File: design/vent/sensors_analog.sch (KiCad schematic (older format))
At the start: 11 parts, among them J14 Conn_01x02, J15 Conn_01x02, J16 Conn_01x03, J17 Conn_01x02, J18 Conn_01x02, U10 SPU01M-15

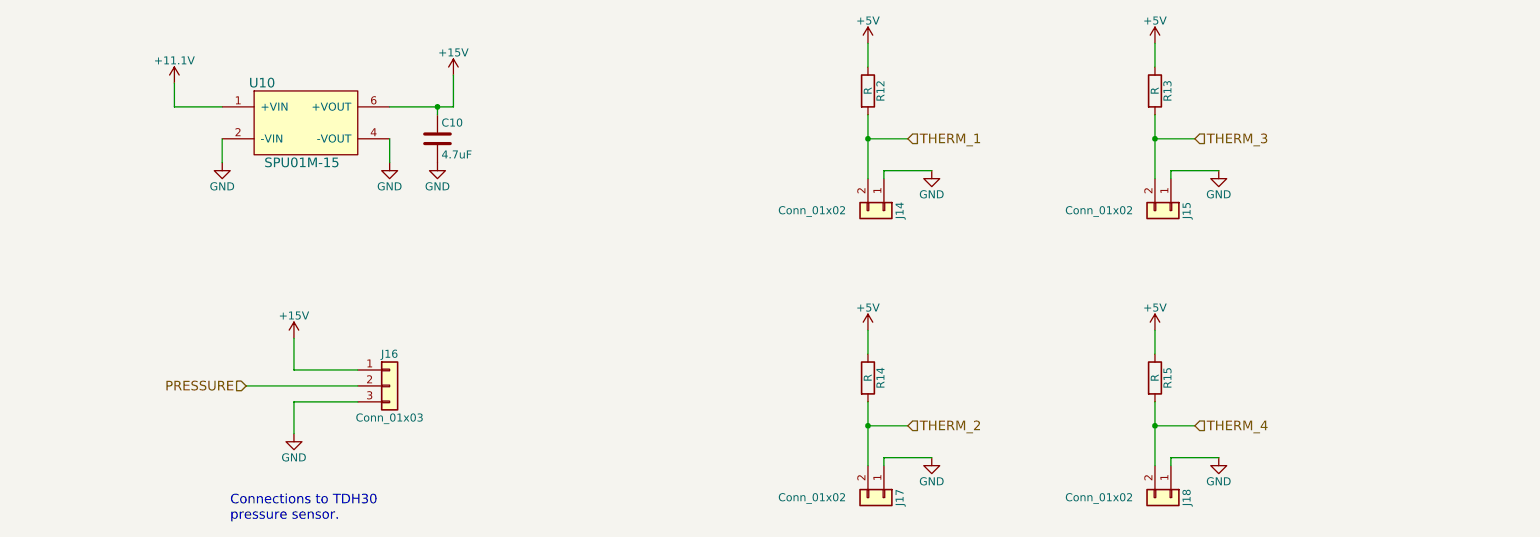
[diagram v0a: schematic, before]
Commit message: Refine schematic
- Add part numbers and correct pinout for mosfets
- Add fuses to battery inputs
- Add decoupling caps to logic translators
- Add flyback diodes to H Bridge, to be populated if the body diodes of
  the mosfets are not sufficient.
- Change H Bridge to operate with 4 inputs instead of 2.

Also, misc directory cleanup.
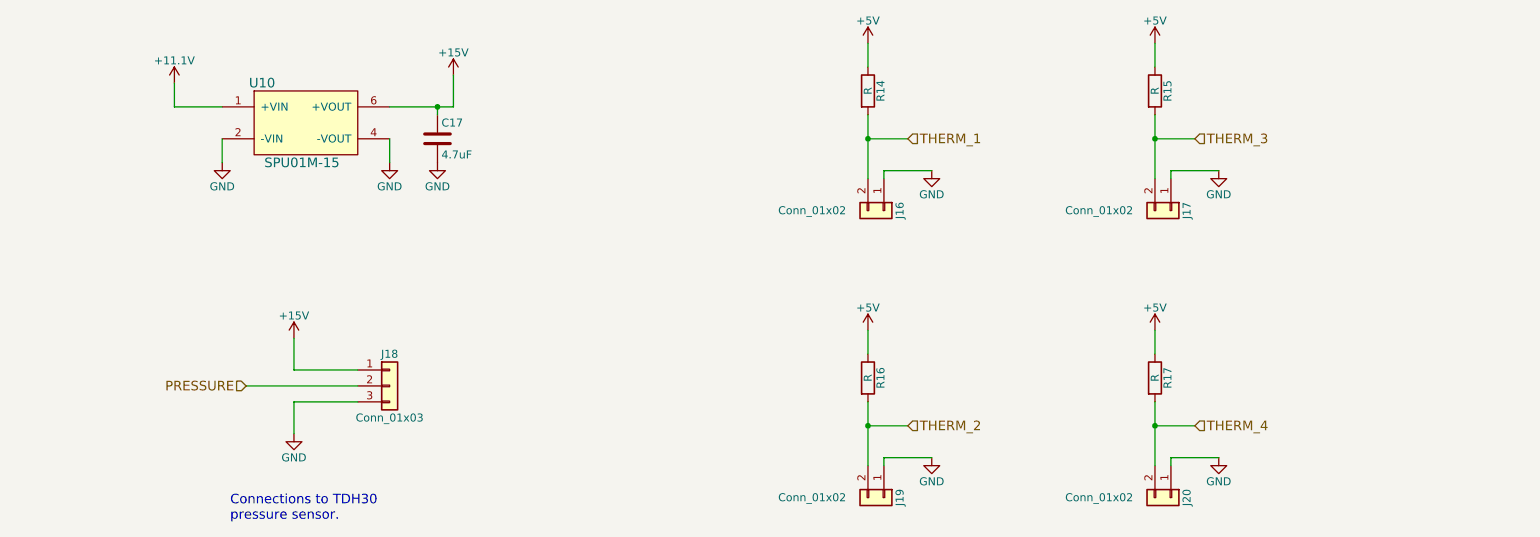
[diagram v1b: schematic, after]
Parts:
- renumbered C10 to C17, J14 to J16, J15 to J17, J16 to J18, J17 to J19, J18 to J20, R12 to R14, R13 to R15, R14 to R16, R15 to R17
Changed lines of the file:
@@
 $EndDescr
 $Comp
-L Conn_01x02 J14
+L Conn_01x02 J16
 U 1 1 5AE81751
 P 6800 3150
-F 0 "J14" H 6800 3250 50  0000 C CNN
+F 0 "J16" H 6800 3250 50  0000 C CNN
 F 1 "Conn_01x02" V 6800 2700 50  0000 C CNN
 F 2 "Connectors_Phoenix:PhoenixContact_MCV-G_02x3.50mm_Vertical" H 6800 3150 50  0001 C CNN
@@
 $EndComp
 $Comp
-L R R12
+L R R14
 U 1 1 5AE81758
 P 6700 2400
-F 0 "R12" V 6780 2400 50  0000 C CNN
+F 0 "R14" V 6780 2400 50  0000 C CNN
 F 1 "R" V 6700 2400 50  0000 C CNN
 F 2 "Resistors_ThroughHole:R_Axial_DIN0207_L6.3mm_D2.5mm_P10.16mm_Horizontal" V 6630 2400 50  0001 C CNN
@@
 $EndComp
 $Comp
-L GND #PWR67
+L GND #PWR78
 U 1 1 5AE8175F
 P 7100 2900
-F 0 "#PWR67" H 7100 2650 50  0001 C CNN
+F 0 "#PWR78" H 7100 2650 50  0001 C CNN
 F 1 "GND" H 7100 2750 50  0000 C CNN
 F 2 "" H 7100 2900 50  0001 C CNN
@@
 	6800 2900 7100 2900
 $Comp
-L +5V #PWR60
+L +5V #PWR71
 U 1 1 5AE8176B
 P 6700 2100
-F 0 "#PWR60" H 6700 1950 50  0001 C CNN
+F 0 "#PWR71" H 6700 1950 50  0001 C CNN
 F 1 "+5V" H 6700 2240 50  0000 C CNN
 F 2 "" H 6700 2100 50  0001 C CNN
@@
 $EndComp
 $Comp
-L +11.1V #PWR63
+L +11.1V #PWR74
 U 1 1 5AE81C44
 P 2350 2350
-F 0 "#PWR63" H 2350 2200 50  0001 C CNN
+F 0 "#PWR74" H 2350 2200 50  0001 C CNN
 F 1 "+11.1V" H 2350 2490 50  0000 C CNN
 F 2 "" H 2350 2350 50  0001 C CNN
@@
 	2350 2500 2650 2500
 $Comp
-L GND #PWR64
+L GND #PWR75
 U 1 1 5AE81C4C
 P 2650 2850
-F 0 "#PWR64" H 2650 2600 50  0001 C CNN
+F 0 "#PWR75" H 2650 2600 50  0001 C CNN
 F 1 "GND" H 2650 2700 50  0000 C CNN
 F 2 "" H 2650 2850 50  0001 C CNN
@@
 	2650 2850 2650 2700
 $Comp
-L GND #PWR65
+L GND #PWR76
 U 1 1 5AE81C53
 P 3700 2850
-F 0 "#PWR65" H 3700 2600 50  0001 C CNN
+F 0 "#PWR76" H 3700 2600 50  0001 C CNN
 F 1 "GND" H 3700 2700 50  0000 C CNN
 F 2 "" H 3700 2850 50  0001 C CNN
@@
 	3700 2850 3700 2700
 $Comp
-L +15V #PWR62
+L +15V #PWR73
 U 1 1 5AE81C5A
 P 4100 2300
-F 0 "#PWR62" H 4100 2150 50  0001 C CNN
+F 0 "#PWR73" H 4100 2150 50  0001 C CNN
 F 1 "+15V" H 4100 2440 50  0000 C CNN
 F 2 "" H 4100 2300 50  0001 C CNN
@@
 	4100 2500 3700 2500
 $Comp
-L Conn_01x03 J16
+L Conn_01x03 J18
 U 1 1 5AE81C9B
 P 3700 4250
-F 0 "J16" H 3700 4450 50  0000 C CNN
+F 0 "J18" H 3700 4450 50  0000 C CNN
 F 1 "Conn_01x03" H 3700 4050 50  0000 C CNN
 F 2 "" H 3700 4250 50  0001 C CNN
@@
 $EndComp
 $Comp
-L +15V #PWR71
+L +15V #PWR82
 U 1 1 5AE81CFD
 P 3100 3950
-F 0 "#PWR71" H 3100 3800 50  0001 C CNN
+F 0 "#PWR82" H 3100 3800 50  0001 C CNN
 F 1 "+15V" H 3100 4090 50  0000 C CNN
 F 2 "" H 3100 3950 50  0001 C CNN
@@
 	3100 4150 3500 4150
 $Comp
-L GND #PWR72
+L GND #PWR83
 U 1 1 5AE81D2F
 P 3100 4550
-F 0 "#PWR72" H 3100 4300 50  0001 C CNN
+F 0 "#PWR83" H 3100 4300 50  0001 C CNN
 F 1 "GND" H 3100 4400 50  0000 C CNN
 F 2 "" H 3100 4550 50  0001 C CNN
@@
 Connections to TDH30\npressure sensor.
 $Comp
-L Conn_01x02 J17
+L Conn_01x02 J19
 U 1 1 5AE8252C
 P 6800 4950
-F 0 "J17" H 6800 5050 50  0000 C CNN
+F 0 "J19" H 6800 5050 50  0000 C CNN
 F 1 "Conn_01x02" V 6800 4500 50  0000 C CNN
 F 2 "Connectors_Phoenix:PhoenixContact_MCV-G_02x3.50mm_Vertical" H 6800 4950 50  0001 C CNN
@@
 $EndComp
 $Comp
-L R R14
+L R R16
 U 1 1 5AE82533
 P 6700 4200
-F 0 "R14" V 6780 4200 50  0000 C CNN
+F 0 "R16" V 6780 4200 50  0000 C CNN
 F 1 "R" V 6700 4200 50  0000 C CNN
 F 2 "Resistors_ThroughHole:R_Axial_DIN0207_L6.3mm_D2.5mm_P10.16mm_Horizontal" V 6630 4200 50  0001 C CNN
@@
 $EndComp
 $Comp
-L GND #PWR73
+L GND #PWR84
 U 1 1 5AE8253A
 P 7100 4700
-F 0 "#PWR73" H 7100 4450 50  0001 C CNN
+F 0 "#PWR84" H 7100 4450 50  0001 C CNN
 F 1 "GND" H 7100 4550 50  0000 C CNN
 F 2 "" H 7100 4700 50  0001 C CNN
@@
 	6800 4700 7100 4700
 $Comp
-L +5V #PWR69
+L +5V #PWR80
 U 1 1 5AE82545
 P 6700 3900
-F 0 "#PWR69" H 6700 3750 50  0001 C CNN
+F 0 "#PWR80" H 6700 3750 50  0001 C CNN
 F 1 "+5V" H 6700 4040 50  0000 C CNN
 F 2 "" H 6700 3900 50  0001 C CNN
@@
 	6700 3900 6700 4050
 $Comp
-L Conn_01x02 J15
+L Conn_01x02 J17
 U 1 1 5AE825CB
 P 8600 3150
-F 0 "J15" H 8600 3250 50  0000 C CNN
+F 0 "J17" H 8600 3250 50  0000 C CNN
 F 1 "Conn_01x02" V 8600 2700 50  0000 C CNN
 F 2 "Connectors_Phoenix:PhoenixContact_MCV-G_02x3.50mm_Vertical" H 8600 3150 50  0001 C CNN
@@
 $EndComp
 $Comp
-L R R13
+L R R15
 U 1 1 5AE825D2
 P 8500 2400
-F 0 "R13" V 8580 2400 50  0000 C CNN
+F 0 "R15" V 8580 2400 50  0000 C CNN
 F 1 "R" V 8500 2400 50  0000 C CNN
 F 2 "Resistors_ThroughHole:R_Axial_DIN0207_L6.3mm_D2.5mm_P10.16mm_Horizontal" V 8430 2400 50  0001 C CNN
@@
 $EndComp
 $Comp
-L GND #PWR68
+L GND #PWR79
 U 1 1 5AE825D9
 P 8900 2900
-F 0 "#PWR68" H 8900 2650 50  0001 C CNN
+F 0 "#PWR79" H 8900 2650 50  0001 C CNN
 F 1 "GND" H 8900 2750 50  0000 C CNN
 F 2 "" H 8900 2900 50  0001 C CNN
@@
 	8600 2900 8900 2900
 $Comp
-L +5V #PWR61
+L +5V #PWR72
 U 1 1 5AE825E4
 P 8500 2100
-F 0 "#PWR61" H 8500 1950 50  0001 C CNN
+F 0 "#PWR72" H 8500 1950 50  0001 C CNN
 F 1 "+5V" H 8500 2240 50  0000 C CNN
 F 2 "" H 8500 2100 50  0001 C CNN
@@
 	8500 2100 8500 2250
 $Comp
-L Conn_01x02 J18
+L Conn_01x02 J20
 U 1 1 5AE82644
 P 8600 4950
-F 0 "J18" H 8600 5050 50  0000 C CNN
+F 0 "J20" H 8600 5050 50  0000 C CNN
 F 1 "Conn_01x02" V 8600 4500 50  0000 C CNN
 F 2 "Connectors_Phoenix:PhoenixContact_MCV-G_02x3.50mm_Vertical" H 8600 4950 50  0001 C CNN
@@
 $EndComp
 $Comp
-L R R15
+L R R17
 U 1 1 5AE8264B
 P 8500 4200
-F 0 "R15" V 8580 4200 50  0000 C CNN
+F 0 "R17" V 8580 4200 50  0000 C CNN
 F 1 "R" V 8500 4200 50  0000 C CNN
 F 2 "Resistors_ThroughHole:R_Axial_DIN0207_L6.3mm_D2.5mm_P10.16mm_Horizontal" V 8430 4200 50  0001 C CNN
@@
 $EndComp
 $Comp
-L GND #PWR74
+L GND #PWR85
 U 1 1 5AE82652
 P 8900 4700
-F 0 "#PWR74" H 8900 4450 50  0001 C CNN
+F 0 "#PWR85" H 8900 4450 50  0001 C CNN
 F 1 "GND" H 8900 4550 50  0000 C CNN
 F 2 "" H 8900 4700 50  0001 C CNN
@@
 	8600 4700 8900 4700
 $Comp
-L +5V #PWR70
+L +5V #PWR81
 U 1 1 5AE8265D
 P 8500 3900
-F 0 "#PWR70" H 8500 3750 50  0001 C CNN
+F 0 "#PWR81" H 8500 3750 50  0001 C CNN
 F 1 "+5V" H 8500 4040 50  0000 C CNN
 F 2 "" H 8500 3900 50  0001 C CNN
@@
 PRESSURE
 $Comp
-L C C10
+L C C17
 U 1 1 5AE95521
 P 4000 2700
-F 0 "C10" H 4025 2800 50  0000 L CNN
+F 0 "C17" H 4025 2800 50  0000 L CNN
 F 1 "4.7uF" H 4025 2600 50  0000 L CNN
 F 2 "" H 4038 2550 50  0001 C CNN
@@
 $EndComp
 $Comp
-L GND #PWR66
+L GND #PWR77
 U 1 1 5AE9556F
 P 4000 2850
-F 0 "#PWR66" H 4000 2600 50  0001 C CNN
+F 0 "#PWR77" H 4000 2600 50  0001 C CNN
 F 1 "GND" H 4000 2700 50  0000 C CNN
 F 2 "" H 4000 2850 50  0001 C CNN

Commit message: Review changes
- Add debug LEDs
- Add pullup resistors on logic shifters for xbee and sd card.
- Add 0 ohm resistor between valve and control power sources (to allow
  for either one of both sources to be used).
- Add another IMU
- Add gate resistors to valve control mosfets
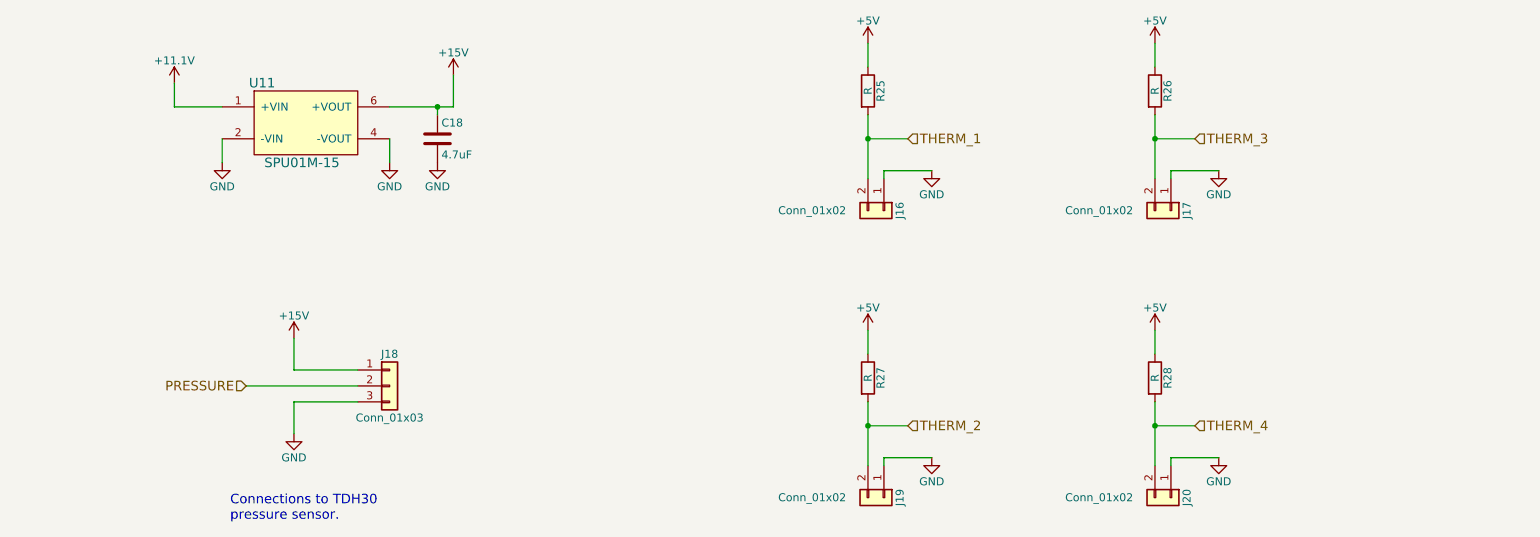
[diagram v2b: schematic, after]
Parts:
- renumbered C17 to C18, R14 to R25, R15 to R26, R16 to R27, R17 to R28, U10 to U11
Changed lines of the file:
@@
 $EndComp
 $Comp
-L R R14
+L R R25
 U 1 1 5AE81758
 P 6700 2400
-F 0 "R14" V 6780 2400 50  0000 C CNN
+F 0 "R25" V 6780 2400 50  0000 C CNN
 F 1 "R" V 6700 2400 50  0000 C CNN
 F 2 "Resistors_ThroughHole:R_Axial_DIN0207_L6.3mm_D2.5mm_P10.16mm_Horizontal" V 6630 2400 50  0001 C CNN
@@
 $EndComp
 $Comp
-L GND #PWR78
+L GND #PWR92
 U 1 1 5AE8175F
 P 7100 2900
-F 0 "#PWR78" H 7100 2650 50  0001 C CNN
+F 0 "#PWR92" H 7100 2650 50  0001 C CNN
 F 1 "GND" H 7100 2750 50  0000 C CNN
 F 2 "" H 7100 2900 50  0001 C CNN
@@
 	6800 2900 7100 2900
 $Comp
-L +5V #PWR71
+L +5V #PWR85
 U 1 1 5AE8176B
 P 6700 2100
-F 0 "#PWR71" H 6700 1950 50  0001 C CNN
+F 0 "#PWR85" H 6700 1950 50  0001 C CNN
 F 1 "+5V" H 6700 2240 50  0000 C CNN
 F 2 "" H 6700 2100 50  0001 C CNN
@@
 	6700 2100 6700 2250
 $Comp
-L SPU01M-15 U10
+L SPU01M-15 U11
 U 1 1 5AE81C3D
 P 3100 2500
-F 0 "U10" H 2900 2650 60  0000 C CNN
+F 0 "U11" H 2900 2650 60  0000 C CNN
 F 1 "SPU01M-15" H 3150 2150 60  0000 C CNN
 F 2 "" H 3100 2500 60  0001 C CNN
@@
 $EndComp
 $Comp
-L +11.1V #PWR74
+L +11.1V #PWR88
 U 1 1 5AE81C44
 P 2350 2350
-F 0 "#PWR74" H 2350 2200 50  0001 C CNN
+F 0 "#PWR88" H 2350 2200 50  0001 C CNN
 F 1 "+11.1V" H 2350 2490 50  0000 C CNN
 F 2 "" H 2350 2350 50  0001 C CNN
@@
 	2350 2500 2650 2500
 $Comp
-L GND #PWR75
+L GND #PWR89
 U 1 1 5AE81C4C
 P 2650 2850
-F 0 "#PWR75" H 2650 2600 50  0001 C CNN
+F 0 "#PWR89" H 2650 2600 50  0001 C CNN
 F 1 "GND" H 2650 2700 50  0000 C CNN
 F 2 "" H 2650 2850 50  0001 C CNN
@@
 	2650 2850 2650 2700
 $Comp
-L GND #PWR76
+L GND #PWR90
 U 1 1 5AE81C53
 P 3700 2850
-F 0 "#PWR76" H 3700 2600 50  0001 C CNN
+F 0 "#PWR90" H 3700 2600 50  0001 C CNN
 F 1 "GND" H 3700 2700 50  0000 C CNN
 F 2 "" H 3700 2850 50  0001 C CNN
@@
 	3700 2850 3700 2700
 $Comp
-L +15V #PWR73
+L +15V #PWR87
 U 1 1 5AE81C5A
 P 4100 2300
-F 0 "#PWR73" H 4100 2150 50  0001 C CNN
+F 0 "#PWR87" H 4100 2150 50  0001 C CNN
 F 1 "+15V" H 4100 2440 50  0000 C CNN
 F 2 "" H 4100 2300 50  0001 C CNN
@@
 $EndComp
 $Comp
-L +15V #PWR82
+L +15V #PWR96
 U 1 1 5AE81CFD
 P 3100 3950
-F 0 "#PWR82" H 3100 3800 50  0001 C CNN
+F 0 "#PWR96" H 3100 3800 50  0001 C CNN
 F 1 "+15V" H 3100 4090 50  0000 C CNN
 F 2 "" H 3100 3950 50  0001 C CNN
@@
 	3100 4150 3500 4150
 $Comp
-L GND #PWR83
+L GND #PWR97
 U 1 1 5AE81D2F
 P 3100 4550
-F 0 "#PWR83" H 3100 4300 50  0001 C CNN
+F 0 "#PWR97" H 3100 4300 50  0001 C CNN
 F 1 "GND" H 3100 4400 50  0000 C CNN
 F 2 "" H 3100 4550 50  0001 C CNN
@@
 $EndComp
 $Comp
-L R R16
+L R R27
 U 1 1 5AE82533
 P 6700 4200
-F 0 "R16" V 6780 4200 50  0000 C CNN
+F 0 "R27" V 6780 4200 50  0000 C CNN
 F 1 "R" V 6700 4200 50  0000 C CNN
 F 2 "Resistors_ThroughHole:R_Axial_DIN0207_L6.3mm_D2.5mm_P10.16mm_Horizontal" V 6630 4200 50  0001 C CNN
@@
 $EndComp
 $Comp
-L GND #PWR84
+L GND #PWR98
 U 1 1 5AE8253A
 P 7100 4700
-F 0 "#PWR84" H 7100 4450 50  0001 C CNN
+F 0 "#PWR98" H 7100 4450 50  0001 C CNN
 F 1 "GND" H 7100 4550 50  0000 C CNN
 F 2 "" H 7100 4700 50  0001 C CNN
@@
 	6800 4700 7100 4700
 $Comp
-L +5V #PWR80
+L +5V #PWR94
 U 1 1 5AE82545
 P 6700 3900
-F 0 "#PWR80" H 6700 3750 50  0001 C CNN
+F 0 "#PWR94" H 6700 3750 50  0001 C CNN
 F 1 "+5V" H 6700 4040 50  0000 C CNN
 F 2 "" H 6700 3900 50  0001 C CNN
@@
 $EndComp
 $Comp
-L R R15
+L R R26
 U 1 1 5AE825D2
 P 8500 2400
-F 0 "R15" V 8580 2400 50  0000 C CNN
+F 0 "R26" V 8580 2400 50  0000 C CNN
 F 1 "R" V 8500 2400 50  0000 C CNN
 F 2 "Resistors_ThroughHole:R_Axial_DIN0207_L6.3mm_D2.5mm_P10.16mm_Horizontal" V 8430 2400 50  0001 C CNN
@@
 $EndComp
 $Comp
-L GND #PWR79
+L GND #PWR93
 U 1 1 5AE825D9
 P 8900 2900
-F 0 "#PWR79" H 8900 2650 50  0001 C CNN
+F 0 "#PWR93" H 8900 2650 50  0001 C CNN
 F 1 "GND" H 8900 2750 50  0000 C CNN
 F 2 "" H 8900 2900 50  0001 C CNN
@@
 	8600 2900 8900 2900
 $Comp
-L +5V #PWR72
+L +5V #PWR86
 U 1 1 5AE825E4
 P 8500 2100
-F 0 "#PWR72" H 8500 1950 50  0001 C CNN
+F 0 "#PWR86" H 8500 1950 50  0001 C CNN
 F 1 "+5V" H 8500 2240 50  0000 C CNN
 F 2 "" H 8500 2100 50  0001 C CNN
@@
 $EndComp
 $Comp
-L R R17
+L R R28
 U 1 1 5AE8264B
 P 8500 4200
-F 0 "R17" V 8580 4200 50  0000 C CNN
+F 0 "R28" V 8580 4200 50  0000 C CNN
 F 1 "R" V 8500 4200 50  0000 C CNN
 F 2 "Resistors_ThroughHole:R_Axial_DIN0207_L6.3mm_D2.5mm_P10.16mm_Horizontal" V 8430 4200 50  0001 C CNN
@@
 $EndComp
 $Comp
-L GND #PWR85
+L GND #PWR99
 U 1 1 5AE82652
 P 8900 4700
-F 0 "#PWR85" H 8900 4450 50  0001 C CNN
+F 0 "#PWR99" H 8900 4450 50  0001 C CNN
 F 1 "GND" H 8900 4550 50  0000 C CNN
 F 2 "" H 8900 4700 50  0001 C CNN
@@
 	8600 4700 8900 4700
 $Comp
-L +5V #PWR81
+L +5V #PWR95
 U 1 1 5AE8265D
 P 8500 3900
-F 0 "#PWR81" H 8500 3750 50  0001 C CNN
+F 0 "#PWR95" H 8500 3750 50  0001 C CNN
 F 1 "+5V" H 8500 4040 50  0000 C CNN
 F 2 "" H 8500 3900 50  0001 C CNN
@@
 PRESSURE
 $Comp
-L C C17
+L C C18
 U 1 1 5AE95521
 P 4000 2700
-F 0 "C17" H 4025 2800 50  0000 L CNN
+F 0 "C18" H 4025 2800 50  0000 L CNN
 F 1 "4.7uF" H 4025 2600 50  0000 L CNN
 F 2 "" H 4038 2550 50  0001 C CNN
@@
 $EndComp
 $Comp
-L GND #PWR77
+L GND #PWR91
 U 1 1 5AE9556F
 P 4000 2850
-F 0 "#PWR77" H 4000 2600 50  0001 C CNN
+F 0 "#PWR91" H 4000 2600 50  0001 C CNN
 F 1 "GND" H 4000 2700 50  0000 C CNN
 F 2 "" H 4000 2850 50  0001 C CNN

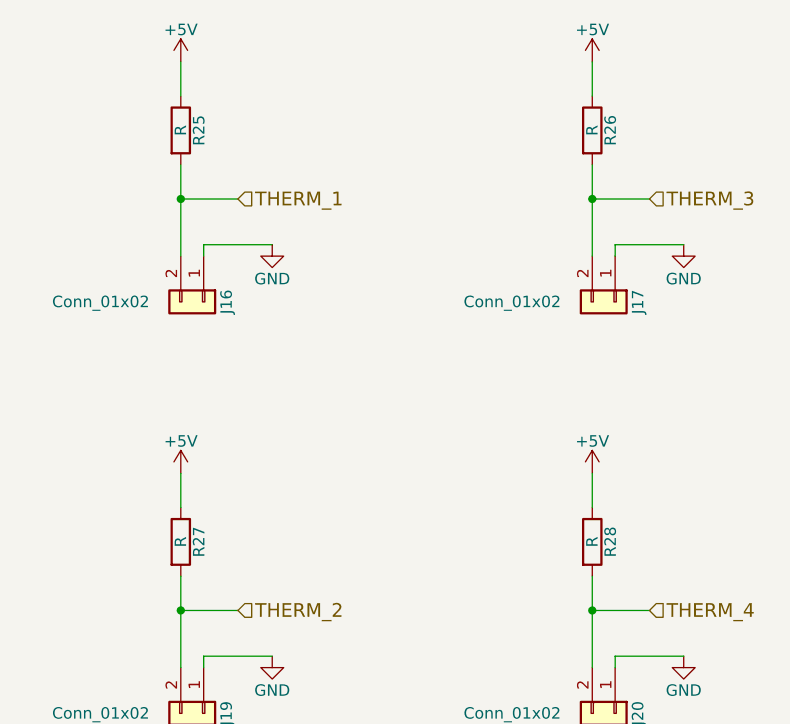
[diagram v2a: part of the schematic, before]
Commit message: Fix MOSFET gate resistors
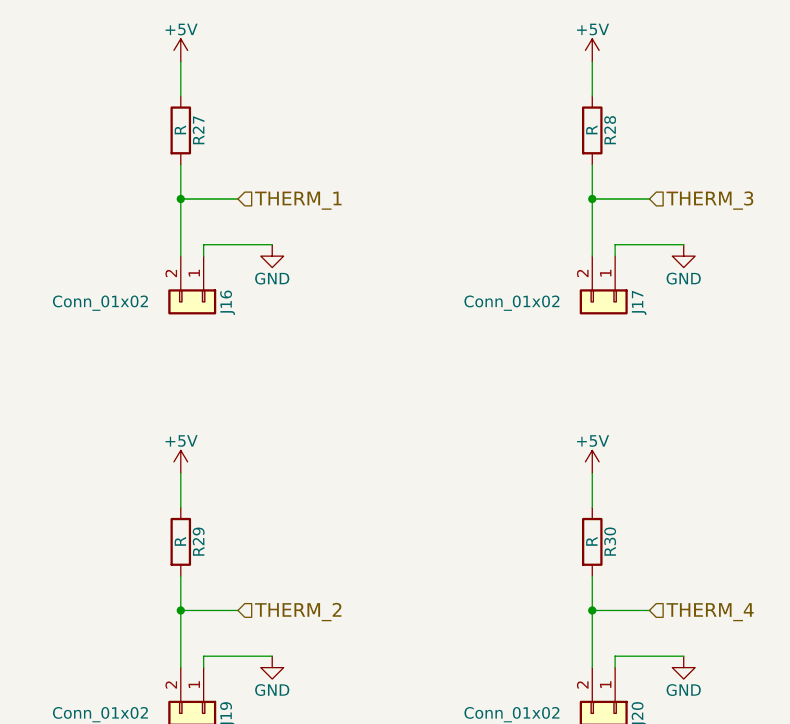
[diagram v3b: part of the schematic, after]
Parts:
- renumbered R25 to R27, R26 to R28, R27 to R29, R28 to R30
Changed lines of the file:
@@
 $EndComp
 $Comp
-L R R25
+L R R27
 U 1 1 5AE81758
 P 6700 2400
-F 0 "R25" V 6780 2400 50  0000 C CNN
+F 0 "R27" V 6780 2400 50  0000 C CNN
 F 1 "R" V 6700 2400 50  0000 C CNN
 F 2 "Resistors_ThroughHole:R_Axial_DIN0207_L6.3mm_D2.5mm_P10.16mm_Horizontal" V 6630 2400 50  0001 C CNN
@@
 $EndComp
 $Comp
-L R R27
+L R R29
 U 1 1 5AE82533
 P 6700 4200
-F 0 "R27" V 6780 4200 50  0000 C CNN
+F 0 "R29" V 6780 4200 50  0000 C CNN
 F 1 "R" V 6700 4200 50  0000 C CNN
 F 2 "Resistors_ThroughHole:R_Axial_DIN0207_L6.3mm_D2.5mm_P10.16mm_Horizontal" V 6630 4200 50  0001 C CNN
@@
 $EndComp
 $Comp
-L R R26
+L R R28
 U 1 1 5AE825D2
 P 8500 2400
-F 0 "R26" V 8580 2400 50  0000 C CNN
+F 0 "R28" V 8580 2400 50  0000 C CNN
 F 1 "R" V 8500 2400 50  0000 C CNN
 F 2 "Resistors_ThroughHole:R_Axial_DIN0207_L6.3mm_D2.5mm_P10.16mm_Horizontal" V 8430 2400 50  0001 C CNN
@@
 $EndComp
 $Comp
-L R R28
+L R R30
 U 1 1 5AE8264B
 P 8500 4200
-F 0 "R28" V 8580 4200 50  0000 C CNN
+F 0 "R30" V 8580 4200 50  0000 C CNN
 F 1 "R" V 8500 4200 50  0000 C CNN
 F 2 "Resistors_ThroughHole:R_Axial_DIN0207_L6.3mm_D2.5mm_P10.16mm_Horizontal" V 8430 4200 50  0001 C CNN
